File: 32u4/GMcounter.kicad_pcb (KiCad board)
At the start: 2 copper layers, 29 parts, among them P1 CONN_01X01, P2 CONN_01X01, P3 CONN_01X01, Q1 MMBT3904, Q2 STL128DN, Q3 MMBT3904, U1 TLC555CP, U2 ATmega32U4, U3 AP1117D33

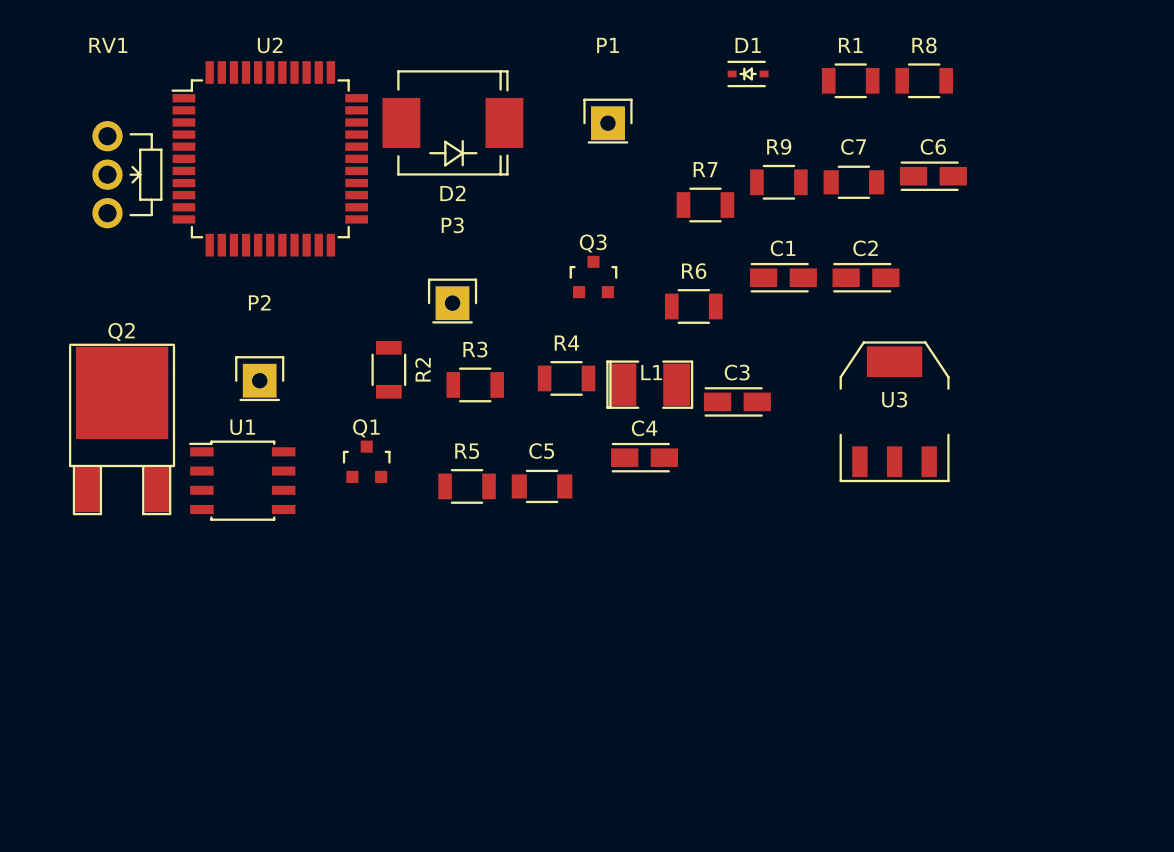
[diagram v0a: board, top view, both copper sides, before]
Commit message: updated with proper resonator footprint
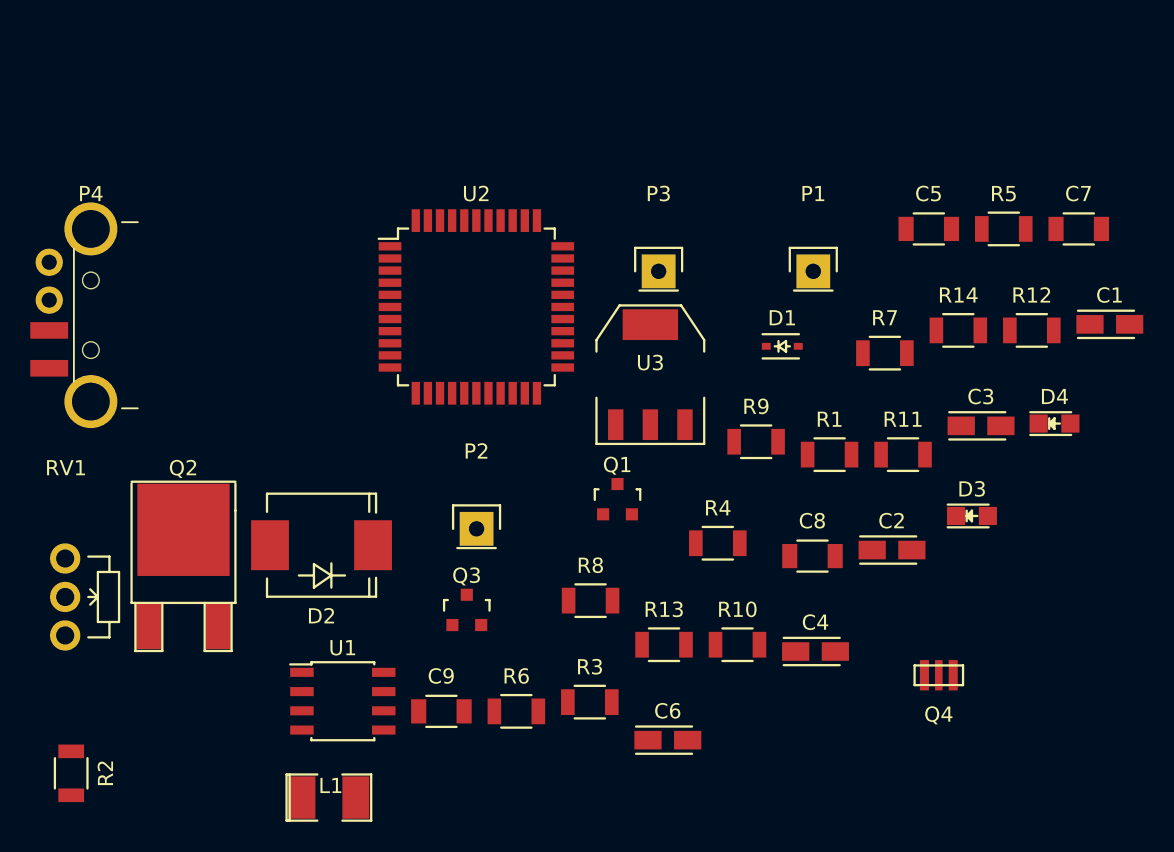
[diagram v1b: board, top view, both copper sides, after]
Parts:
- added C8: 0.1uf, Capacitors_SMD:C_1206, F.Cu at (87.0, 57.9)
- added C9: 0.1uf, Capacitors_SMD:C_1206, F.Cu at (62.5, 68.2)
- added D3: LED, LEDs:LED_0805, F.Cu at (97.6, 55.3)
- added D4: LED, LEDs:LED_0805, F.Cu at (103.0, 49.2)
- added P4: USB_A, USB_oshpark:USB_A_CNCTech_modified_for_oshpark, F.Cu at (46.3, 42.0)
- added Q4: CSTLA_T, MyKiCadLibs:Murata-16mhz-Resonator, F.Cu at (95.4, 65.8)
- added R10: 22, Resistors_SMD:R_1206, F.Cu at (82.1, 63.8)
- added R11: 22, Resistors_SMD:R_1206, F.Cu at (93.0, 51.2)
- added R12: 500, Resistors_SMD:R_1206, F.Cu at (101.5, 43.0)
- added R13: 500, Resistors_SMD:R_1206, F.Cu at (77.2, 63.8)
- added R14: 22, Resistors_SMD:R_1206, F.Cu at (96.7, 43.0)
- moved C6 41.2 mm to (77.5, 70.1)
- moved R8 40.8 mm to (72.4, 60.9)
- moved R5 39.3 mm to (99.7, 36.3)
- moved L1 34.5 mm to (55.1, 73.9)
- moved R2 33.9 mm to (38.1, 72.3)
- moved C5 30.7 mm to (94.7, 36.3)
- moved D2 29.2 mm to (54.6, 57.2)
- moved R6 29.2 mm to (67.5, 68.2)
- moved RV1 28.0 mm to (37.7, 58.1)
- moved R1 24.7 mm to (88.2, 51.2)
- moved Q3 23.5 mm to (64.2, 61.5)
- moved R3 22.3 mm to (72.3, 67.6)
- moved C1 21.8 mm to (106.7, 42.6)
- moved D1 18.1 mm to (85.0, 44.1)
- moved C2 18.1 mm to (92.3, 57.5)
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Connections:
- U2 pad 13: (no net) -> Net-(R14-Pad2)
- U2 pad 14: (no net) -> +5V
- U2 pad 16: (no net) -> Net-(Q4-Pad3)
- U2 pad 17: (no net) -> Net-(Q4-Pad1)
- U2 pad 19: PULSE -> (no net)
- U2 pad 2: (no net) -> +5V
- U2 pad 24: (no net) -> +5V
- U2 pad 3: (no net) -> Net-(R10-Pad2)
- U2 pad 30: (no net) -> PULSE
- U2 pad 34: (no net) -> +5V
- U2 pad 36: (no net) -> Net-(R13-Pad1)
- U2 pad 4: (no net) -> Net-(R11-Pad2)
- U2 pad 42: (no net) -> Net-(C8-Pad1)
- U2 pad 44: (no net) -> +5V
- U2 pad 5: (no net) -> GND
- U2 pad 6: (no net) -> Net-(C9-Pad2)
- U2 pad 7: (no net) -> +5V

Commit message: updates
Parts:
- added D5: one_diode_please, Diodes_SMD:SMA_Standard, B.Cu at (166.0, 68.2)
- added P5: CONN_01X03, Pin_Headers:Pin_Header_Straight_1x03, F.Cu at (125.0, 67.6)
- added P6: CONN_02X04, Pin_Headers:Pin_Header_Straight_2x04, F.Cu at (130.6, 76.2)
- P4: footprint USB_oshpark:USB_A_CNCTech_modified_for_oshpark -> MyKiCadLibs:USB_Micro-B-OshPark
- R14: value 22 -> 10k
- moved P4 137.9 mm to (181.0, 71.5), turned to 90 degrees
- moved U3 93.4 mm to (165.9, 72.6), turned to 180 degrees
- moved R10 92.5 mm to (174.4, 70.6), turned to 180 degrees
- moved R11 84.3 mm to (174.2, 73.9), turned to 180 degrees
- moved U2 83.0 mm to (142.5, 70.7), turned to 45 degrees
- moved C6 80.9 mm to (158.4, 68.2), turned to 270 degrees
- moved R13 80.0 mm to (155.9, 78.5)
- moved C5 74.0 mm to (158.4, 74.0), turned to 90 degrees
- moved C4 68.4 mm to (154.9, 73.9), turned to 90 degrees
- moved RV1 66.8 mm to (104.3, 63.5)
- moved D4 65.0 mm to (161.0, 78.5), turned to 180 degrees
- moved C7 59.6 mm to (155.1, 68.1), turned to 270 degrees
- moved C9 56.1 mm to (118.0, 76.9), turned to 90 degrees
- moved Q4 55.8 mm to (149.6, 78.7), turned to 45 degrees
- moved Q2 54.8 mm to (99.9, 68.8), turned to 90 degrees
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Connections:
- net Net-(R14-Pad2) renamed RST
- L1 pad 2: +3V3 -> Net-(L1-Pad2)
- P4 pad 1: +5V -> Net-(D5-Pad1)
- R4 pad 2: +3V3 -> Net-(L1-Pad2)
- U1 pad 8: +3V3 -> Net-(L1-Pad2)
- U2 pad 10: (no net) -> MOSI
- U2 pad 11: (no net) -> MISO
- U2 pad 18: (no net) -> SCL
- U2 pad 19: (no net) -> SDA
- U2 pad 9: (no net) -> SCLK
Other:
- board outline added: 120.4 x 21.8 mm

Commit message: updates
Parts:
- added P7: CONN_01X03, Pin_Headers:Pin_Header_Straight_1x03, F.Cu at (180.3, 79.2)
- moved P2 99.1 mm to (162.6, 57.4)
- moved C3 82.4 mm to (166.6, 63.0), turned to 0 degrees
- moved R7 80.4 mm to (161.0, 63.0), turned to 0 degrees
- moved R8 74.7 mm to (156.0, 63.0), turned to 0 degrees
- moved Q3 60.5 mm to (171.7, 63.0), turned to 0 degrees
- moved P3 34.5 mm to (150.9, 63.5)
- moved P5 28.1 mm to (98.6, 77.2), turned to 180 degrees
- moved Q1 27.8 mm to (83.4, 68.6), turned to 0 degrees
- moved R4 27.1 mm to (83.8, 63.5), turned to 0 degrees
- moved Q2 25.6 mm to (75.4, 76.2)
- moved RV1 24.7 mm to (84.8, 78.7), turned to 270 degrees
- moved C2 23.5 mm to (67.1, 69.1)
- moved R5 20.3 mm to (81.3, 73.7), turned to 180 degrees
- moved R9 18.5 mm to (128.1, 63.9), turned to 180 degrees
- moved L1 18.0 mm to (103.6, 65.5), turned to 90 degrees
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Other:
- board size 120.4 x 21.8 mm -> 120.4 x 29 mm
- board text added: "SBM-20 size"
- board text added: "SI-3BG Size"

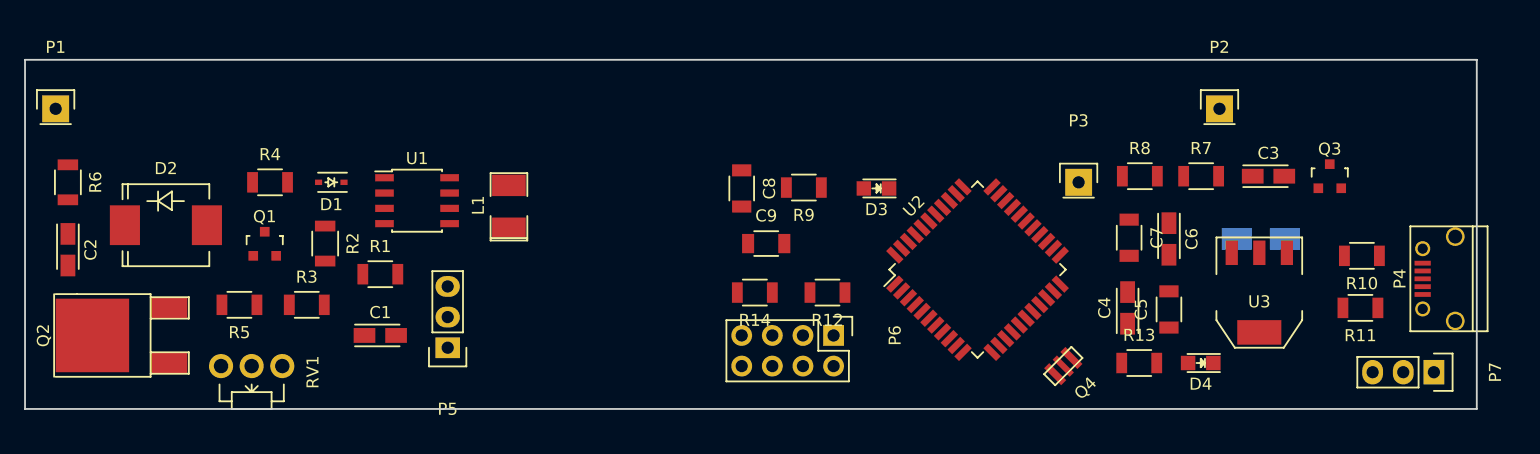
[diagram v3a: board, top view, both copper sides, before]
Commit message: changed foot print for inductor, changed design rules
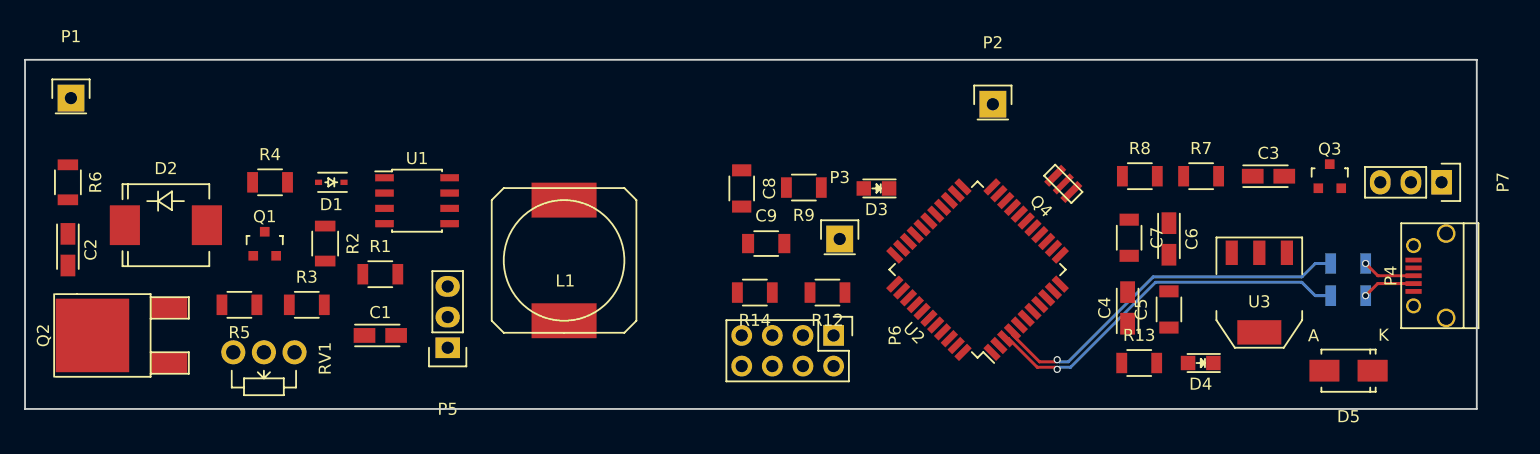
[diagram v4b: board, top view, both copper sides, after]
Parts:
- D5: moved to F.Cu
- L1: footprint SMD_Packages:SMD-1210_Pol -> Inductors:SELF-WE-PD-XXL
- R10, R11: moved to B.Cu
- moved P3 20.4 mm to (131.1, 68.2)
- moved P2 18.8 mm to (143.8, 57.0)
- moved P7 15.8 mm to (181.0, 63.5)
- moved Q4 15.1 mm to (149.6, 63.6), turned to 315 degrees
- moved D5 13.1 mm to (173.3, 79.1)
- moved L1 6.38 mm to (108.2, 70.0)
- moved P1 1.55 mm to (67.3, 56.5)
- moved RV1 1.53 mm to (85.9, 77.6)
- moved R11 1.44 mm to (173.2, 72.9)
- moved R10 1.31 mm to (173.2, 70.2)
- moved P4 0.80 mm to (180.2, 71.2)
- turned U2 to 135 degrees
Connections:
- R10 pad 2: Net-(R10-Pad2) -> MCD+
- R11 pad 2: Net-(R11-Pad2) -> MCD-
- U2 pad 3: Net-(R10-Pad2) -> MCD-
- U2 pad 4: Net-(R11-Pad2) -> MCD+
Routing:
- net MCD-: track 0.00 -> 31.5 mm, vias 0 -> 1
- net MCD+: track 0.00 -> 31.1 mm, vias 0 -> 1
- net D+: track 0.00 -> 4.40 mm, vias 0 -> 1
- net D-: track 0.00 -> 4.39 mm, vias 0 -> 1
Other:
- net class HighV added: clearance 0.6, trace_width 0.25, via_dia 0.6, via_drill 0.4
- net class highA added: clearance 0.2, trace_width 0.5, via_dia 0.6, via_drill 0.4

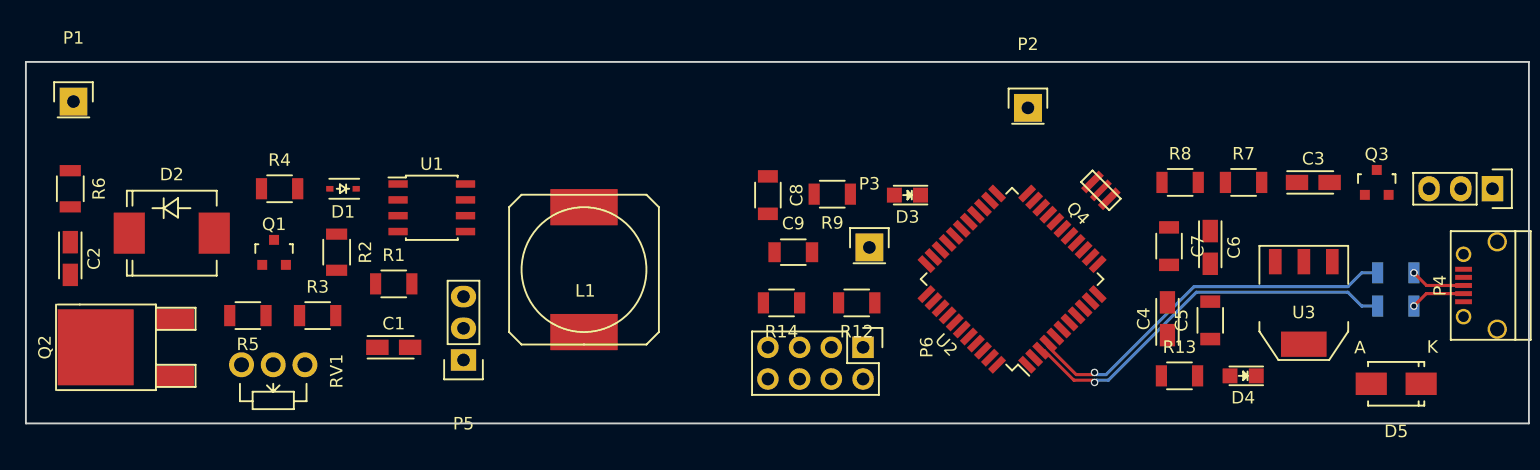
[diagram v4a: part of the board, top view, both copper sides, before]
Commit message: some manual routing for diff pairs and crystal
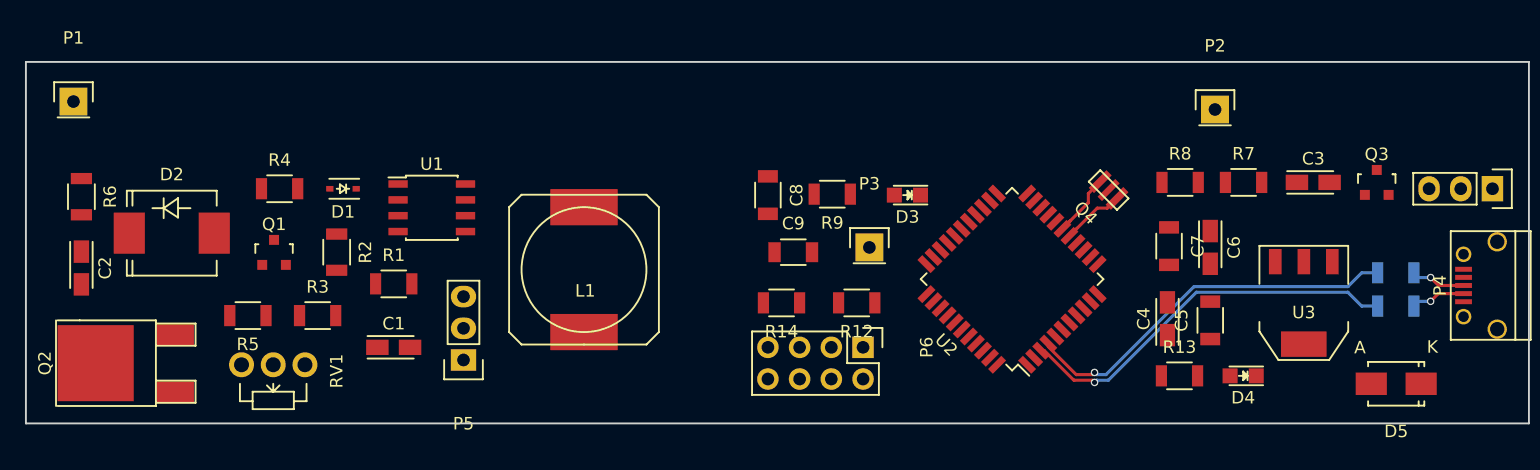
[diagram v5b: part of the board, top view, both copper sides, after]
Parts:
- moved P2 15.0 mm to (158.8, 57.1)
- moved Q2 1.27 mm to (75.4, 77.5)
- moved C2 1.17 mm to (67.9, 69.8)
- moved R6 1.09 mm to (67.9, 64.1)
- moved Q4 0.62 mm to (150.2, 63.6)
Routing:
- net Net-(Q4-Pad3): track 0.00 -> 5.05 mm
- net Net-(Q4-Pad1): track 0.00 -> 5.03 mm
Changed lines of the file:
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@@
     (thickness 1.6)
     (drawings 11)
-    (tracks 28)
+    (tracks 41)
     (zones 0)
     (modules 44)
@@
   )
   (module Capacitors_Tantalum_SMD:TantalC_SizeA_EIA-3216_Reflow (layer F.Cu)
-    (at 67.056 69.088 270)
+    (at 67.945 69.85 270)
     (descr "Tantal Cap. , Size A, EIA-3216, Reflow")
     (tags "Tantal Capacitor Size-A EIA-3216 reflow")
@@
   )
   (module Resistors_SMD:R_1206 (layer F.Cu)
-    (at 67.056 63.5 270)
+    (at 67.945 64.135 270)
     (descr "Resistor SMD 1206, reflow soldering, Vishay (see dcrcw.pdf)")
     (tags "resistor 1206")
@@
   )
   (module TO_SOT_Packages_SMD:TO-252-2Lead (layer F.Cu)
-    (at 75.438 76.2 90)
+    (at 75.438 77.47 90)
     (descr "DPAK / TO-252 2-lead smd package")
     (tags "dpak TO-252")
@@
   )
   (module MyKiCadLibs:Murata-16mhz-Resonator (layer F.Cu)
-    (at 149.606 63.627 315)
+    (at 150.2283 63.6016 315)
     (fp_text reference Q4 (at 0 2.6 315) (layer F.SilkS)
       (effects (font (size 1 1) (thickness 0.15)))
@@
   )
   (module Pin_Headers:Pin_Header_Straight_1x01 (layer F.Cu)
-    (at 143.764 57.023)
+    (at 158.75 57.15)
     (descr "Through hole pin header")
     (tags "pin header")
@@
   (gr_line (start 183.896 53.34) (end 183.896 82.296) (layer Edge.Cuts) (width 0.15))
   (gr_line (start 63.5 53.34) (end 183.896 53.34) (layer Edge.Cuts) (width 0.15))
-  (segment (start 178.656 71.897) (end 175.679 71.897) (width 0.25) (layer F.Cu) (net 21))
-  (segment (start 175.679 71.897) (end 174.678 72.898) (width 0.25) (layer F.Cu) (net 21))
-  (via (at 174.678 72.898) (size 0.6) (drill 0.4) (layers F.Cu B.Cu) (net 21))
-  (segment (start 178.656 71.247) (end 175.694 71.247) (width 0.25) (layer F.Cu) (net 22))
-  (segment (start 175.694 71.247) (end 174.678 70.231) (width 0.25) (layer F.Cu) (net 22))
-  (via (at 174.678 70.231) (size 0.6) (drill 0.4) (layers F.Cu B.Cu) (net 22))
+  (segment (start 176.022 72.517) (end 175.059 72.517) (width 0.25) (layer B.Cu) (net 21))
+  (segment (start 175.059 72.517) (end 174.678 72.898) (width 0.25) (layer B.Cu) (net 21))
+  (segment (start 178.656 71.897) (end 176.642 71.897) (width 0.25) (layer F.Cu) (net 21))
+  (segment (start 176.642 71.897) (end 176.022 72.517) (width 0.25) (layer F.Cu) (net 21))
+  (via (at 176.022 72.517) (size 0.6) (drill 0.4) (layers F.Cu B.Cu) (net 21))
+  (segment (start 176.022 70.612) (end 175.059 70.612) (width 0.25) (layer B.Cu) (net 22))
+  (segment (start 175.059 70.612) (end 174.678 70.231) (width 0.25) (layer B.Cu) (net 22))
+  (segment (start 176.657 71.247) (end 176.022 70.612) (width 0.25) (layer F.Cu) (net 22))
+  (via (at 176.022 70.612) (size 0.6) (drill 0.4) (layers F.Cu B.Cu) (net 22))
+  (segment (start 178.656 71.247) (end 176.657 71.247) (width 0.25) (layer F.Cu) (net 22))
+  (segment (start 148.6027 64.6176) (end 148.6027 63.883698) (width 0.25) (layer F.Cu) (net 23))
+  (segment (start 148.6027 63.883698) (end 149.556549 62.929849) (width 0.25) (layer F.Cu) (net 23))
+  (segment (start 147.125549 66.094751) (end 148.6027 64.6176) (width 0.25) (layer F.Cu) (net 23))
+  (segment (start 146.524509 66.708491) (end 147.125549 66.107451) (width 0.25) (layer F.Cu) (net 23))
+  (segment (start 147.125549 66.107451) (end 147.125549 66.094751) (width 0.25) (layer F.Cu) (net 23))
+  (segment (start 150.900051 64.273351) (end 150.122234 65.051168) (width 0.25) (layer F.Cu) (net 24))
+  (segment (start 150.122234 65.051168) (end 149.313203 65.051168) (width 0.25) (layer F.Cu) (net 24))
+  (segment (start 149.313203 65.051168) (end 147.691234 66.673137) (width 0.25) (layer F.Cu) (net 24))
+  (segment (start 147.691234 66.673137) (end 147.090194 67.274177) (width 0.25) (layer F.Cu) (net 24))
   (segment (start 149.098 78.213) (end 148.922999 78.388001) (width 0.25) (layer F.Cu) (net 34))
   (segment (start 145.393138 76.148367) (end 145.393138 75.90088) (width 0.25) (layer F.Cu) (net 34) (status 30))

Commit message: pre-5.0 test
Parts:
- moved P2 12.7 mm to (146.1, 57.1)
- moved R8 5.34 mm to (161.3, 62.9), turned to 180 degrees
- moved R7 4.83 mm to (156.2, 62.9), turned to 180 degrees
- moved R1 1.33 mm to (93.3, 72.4)
- moved C1 0.74 mm to (93.3, 76.8)
- moved P1 0.63 mm to (67.3, 57.1)
- moved R2 0.51 mm to (88.9, 68.6)
- moved Q1 0.44 mm to (83.8, 68.6)
- moved D2 0.38 mm to (75.6, 67.1)
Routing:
- net GND: track 0.00 -> 5.55 mm
